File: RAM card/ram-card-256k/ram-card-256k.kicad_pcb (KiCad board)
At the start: 2 copper layers, 41.9 x 53.3 mm, 12 parts, among them J1 RAM card connector, U1 HC138, U2 KM681000BLG, U3 KM681000BLG

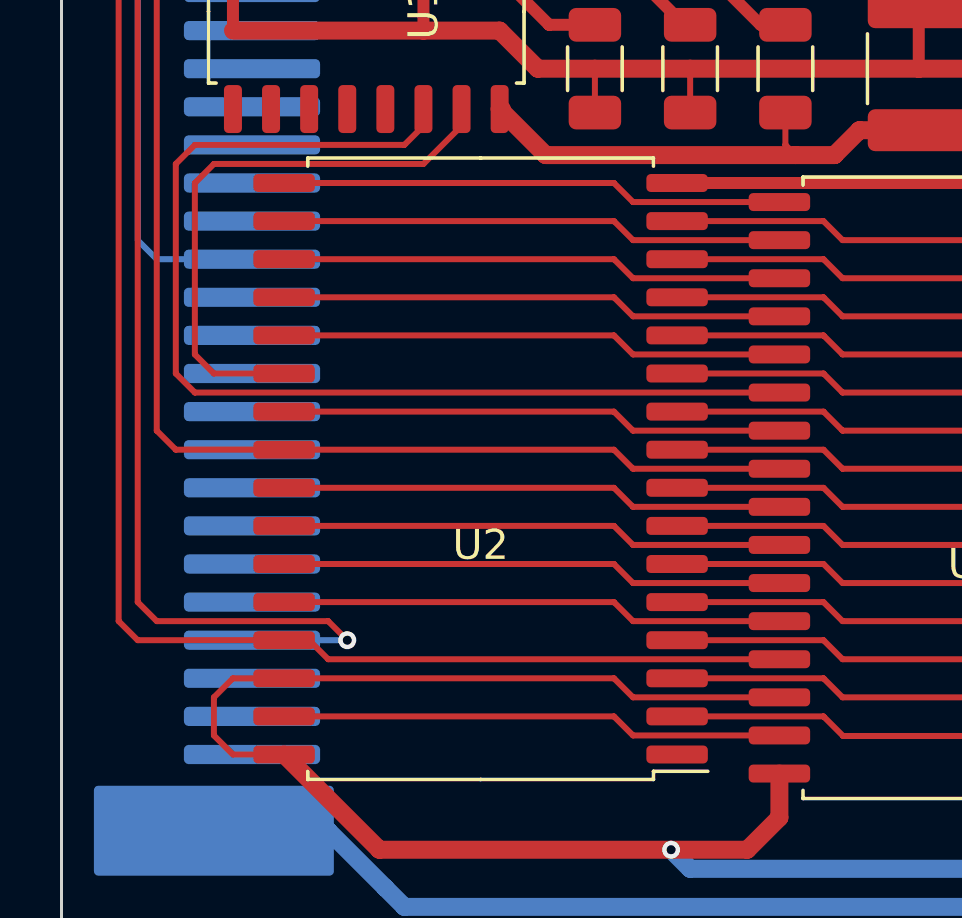
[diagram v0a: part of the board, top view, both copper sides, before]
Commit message: Layout Data bus
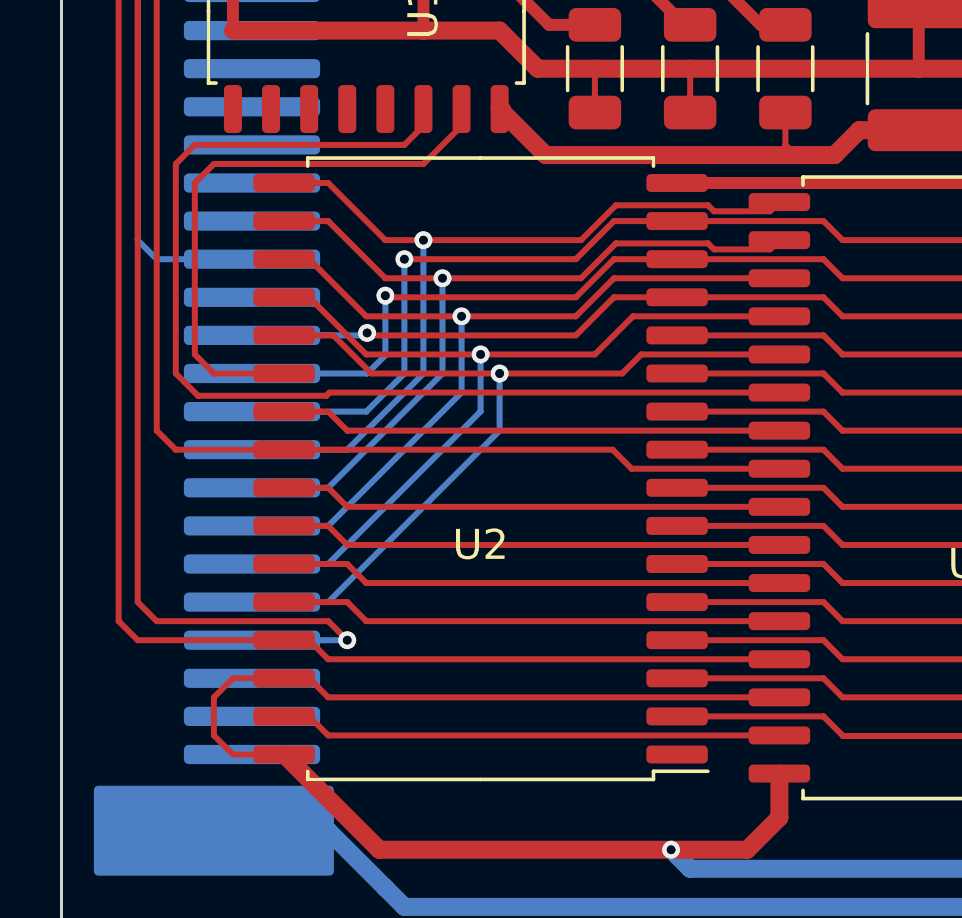
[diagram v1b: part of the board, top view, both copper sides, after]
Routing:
- net /D2: track 16.8 -> 35.8 mm, vias 0 -> 1
- net /D1: track 16.3 -> 33.3 mm, vias 0 -> 1
- net /D0: track 16.8 -> 31.5 mm, vias 0 -> 1
- net /D7: track 16.8 -> 29.8 mm, vias 0 -> 1
- net /D6: track 16.8 -> 29.5 mm, vias 0 -> 1
- net /D3: track 16.8 -> 29.2 mm, vias 0 -> 1
- net /D5: track 16.8 -> 29.2 mm, vias 0 -> 1
- net /D4: track 16.8 -> 29.1 mm, vias 0 -> 1

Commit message: Data bus
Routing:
- net /D5: track 29.2 -> 43.0 mm
- net /D7: track 29.8 -> 42.5 mm
- net /D6: track 29.5 -> 40.8 mm
- net /D3: track 29.2 -> 31.2 mm
- net /D4: track 29.1 -> 31.1 mm
- net /D2: track 35.8 -> 36.9 mm

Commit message: No errors, no warnings
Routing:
- net /A0: track 16.8 -> 93.2 mm, vias 0 -> 1
- net /A1: track 16.8 -> 86.3 mm, vias 0 -> 1
- net /A2: track 16.8 -> 79.4 mm, vias 0 -> 1
- net /A16: track 16.8 -> 74.6 mm, vias 0 -> 1
- net /A14: track 16.8 -> 73.1 mm, vias 0 -> 1
- net /A12: track 16.8 -> 70.9 mm, vias 0 -> 1
- net /A8: track 16.8 -> 68.3 mm, vias 0 -> 1
- net /A15: track 16.8 -> 67.8 mm, vias 0 -> 1
- net /A7: track 16.8 -> 65.3 mm, vias 0 -> 1
- net /A3: track 16.8 -> 65.3 mm, vias 0 -> 1
- net /A9: track 16.8 -> 65.2 mm, vias 0 -> 1
- net /A4: track 16.8 -> 65.0 mm, vias 0 -> 1
- net /A13: track 16.8 -> 65.0 mm, vias 0 -> 1
- net /A6: track 16.8 -> 65.0 mm, vias 0 -> 1
- net /A5: track 16.8 -> 64.8 mm, vias 0 -> 1
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
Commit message: Layout
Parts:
- U1: footprint Package_SO:SOP-16_4.55x10.3mm_P1.27mm -> Package_SO:SOP-16_3.9x9.9mm_P1.27mm
- moved J1 1.02 mm to (121.7, 64.8)
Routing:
- net GND: track 193.9 -> 175.6 mm
- net /A12: track 70.9 -> 60.0 mm
- net R/W: track 83.8 -> 81.3 mm
- net Net-(D1-Pad2): track 59.6 -> 61.9 mm
- net VCC: track 113.0 -> 110.8 mm
- net /A11: track 60.4 -> 62.0 mm
- net Net-(U1-Pad14): track 36.7 -> 35.2 mm
- net /A8: track 68.3 -> 69.8 mm
- net Net-(U1-Pad15): track 18.1 -> 16.9 mm
- net /A9: track 65.2 -> 66.3 mm
- net /A7: track 65.3 -> 64.2 mm
- net /A16: track 74.6 -> 73.7 mm
- net Net-(J1-Pad3): track 19.0 -> 19.9 mm
- net /A14: track 73.1 -> 72.2 mm
- net Net-(J1-Pad21): track 45.5 -> 44.6 mm
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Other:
- board size 41.9 x 53.3 mm -> 41.9 x 54.1 mm
- board text added: "CR1216"
- board text added: "R/W"

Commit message: Version 1.0
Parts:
- BT1: footprint custom-footprints:Battery_CR1216 -> custom-footprints:Battery_CR1216_hole
- moved BT1 3.21 mm to (141.7, 49.6)
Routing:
- net Net-(BT1-Pad1): track 5.49 -> 12.1 mm, vias 0 -> 1
- net GND: track 175.6 -> 180.8 mm
- net Net-(J1-Pad21): track 44.6 -> 47.2 mm
- net /A13: track 64.2 -> 62.4 mm
- net /A0: track 94.0 -> 92.5 mm
- net R/W: track 81.3 -> 79.9 mm
- net /A1: track 86.7 -> 85.6 mm
- net /A16: track 73.7 -> 72.7 mm
- net /A2: track 79.4 -> 78.6 mm
- net /A9: track 66.3 -> 65.6 mm
- net /A7: track 64.2 -> 63.5 mm
- net /A5: track 64.8 -> 64.0 mm
- net /A4: track 65.0 -> 64.3 mm
- net /A11: track 62.0 -> 61.3 mm
- net /A10: track 60.7 -> 60.0 mm
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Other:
- board text added: "CR1216 / 3Volt"
- board text added: "v1.0"
- board text removed: "CR1216"
